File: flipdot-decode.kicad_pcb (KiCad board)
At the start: 2 copper layers, 44 x 19 mm, 10 parts, among them J1 Conn_01x05_Pin, J2 Conn_01x06_Pin, J3 Conn_01x03_Pin, SW1 SW_DIP_x05, U2 MAX485E, U3 CH32V003FxPx

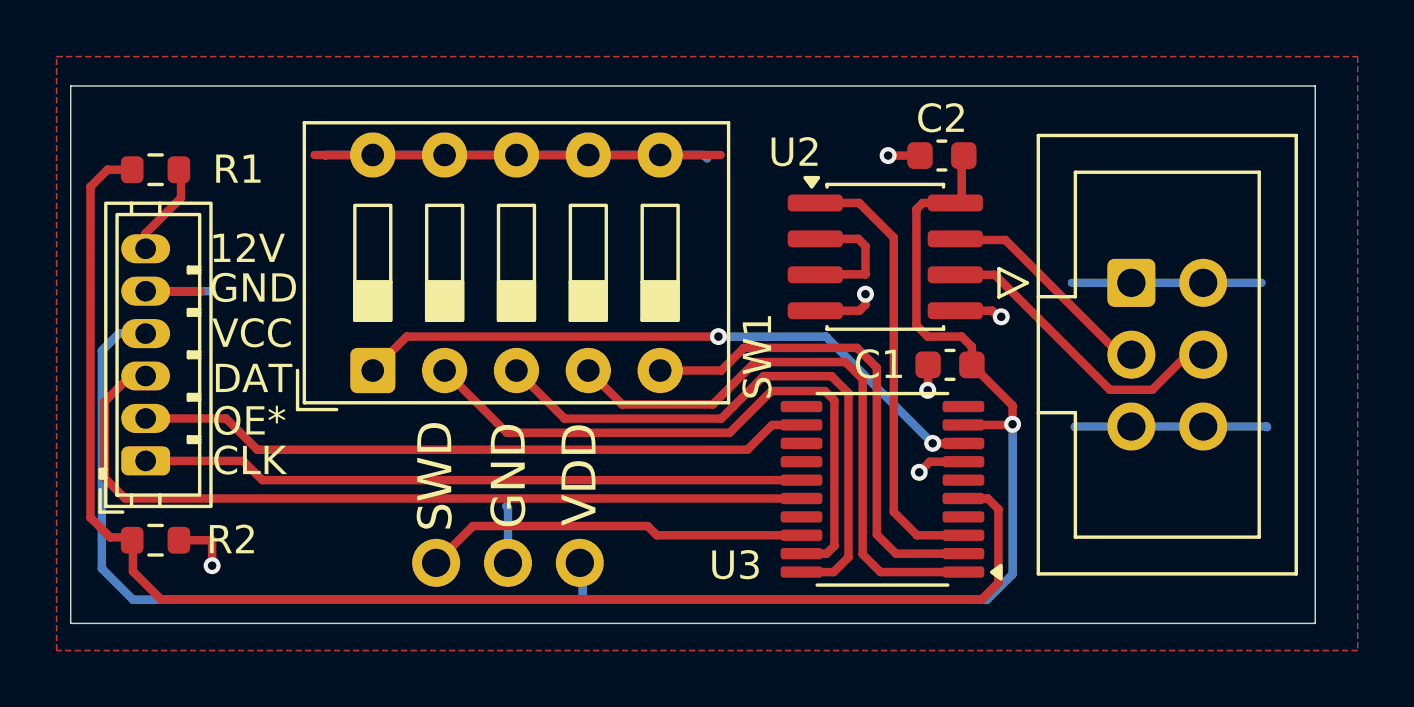
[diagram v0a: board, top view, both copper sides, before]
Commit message: add reset pin
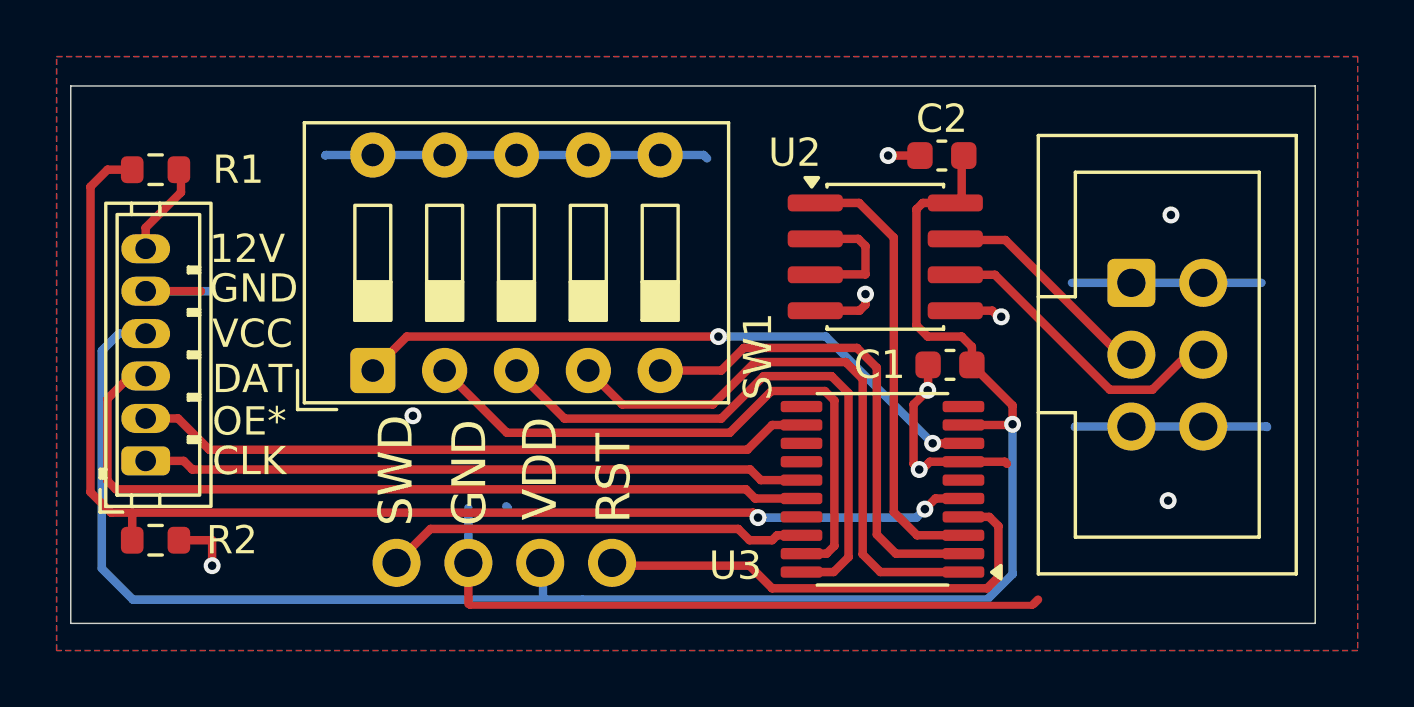
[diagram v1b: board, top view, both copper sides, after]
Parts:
- J3: value Conn_01x03_Pin -> Conn_01x04_Pin; footprint Connector_PinHeader_2.54mm:PinHeader_1x03_P2.54mm_Vertical -> Connector_PinHeader_2.54mm:PinHeader_1x04_P2.54mm_Vertical
- R1: value R_Small -> 470K
- R2: value R_Small -> 150K
- moved J3 1.14 mm to (119.6, 78.9)
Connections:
- J3 pad 1: VCC -> /NRST
- J3 pad 2: GND -> VCC
- J3 pad 3: /SWD -> GND
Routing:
- net /NRST: track 0.00 -> 17.4 mm
- net GND: track 62.1 -> 74.0 mm, vias 6 -> 9
- net /VBAT: track 51.8 -> 45.2 mm, vias 0 -> 2
- net /SWD: track 13.6 -> 15.1 mm
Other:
- board text added: "2026-05-20"
- board text added: "RST"
